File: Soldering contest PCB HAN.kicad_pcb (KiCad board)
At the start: 2 copper layers, 99.1 x 98.6 mm, 18 parts, among them J1 Screw_Terminal_01x02, Q1 2N3904, Q2 2N3904

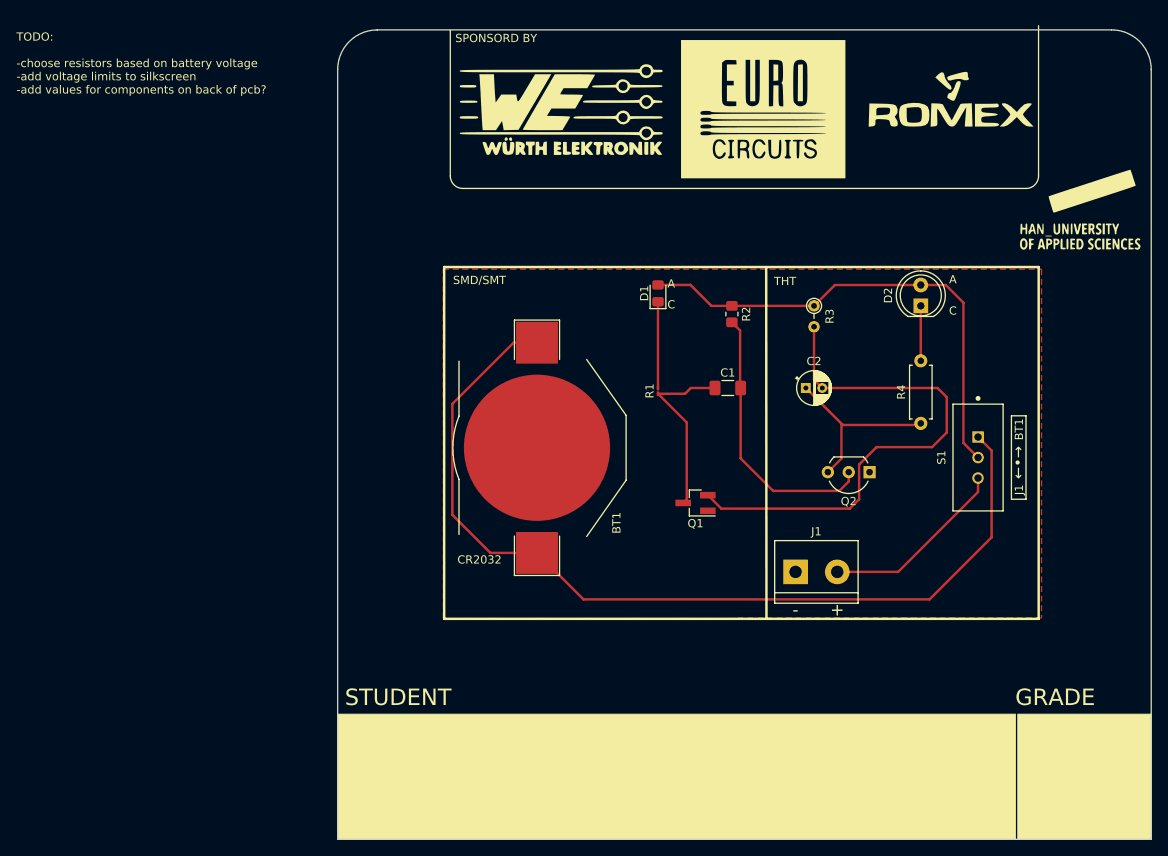
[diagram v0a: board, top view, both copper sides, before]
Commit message: added component values to silkscreen
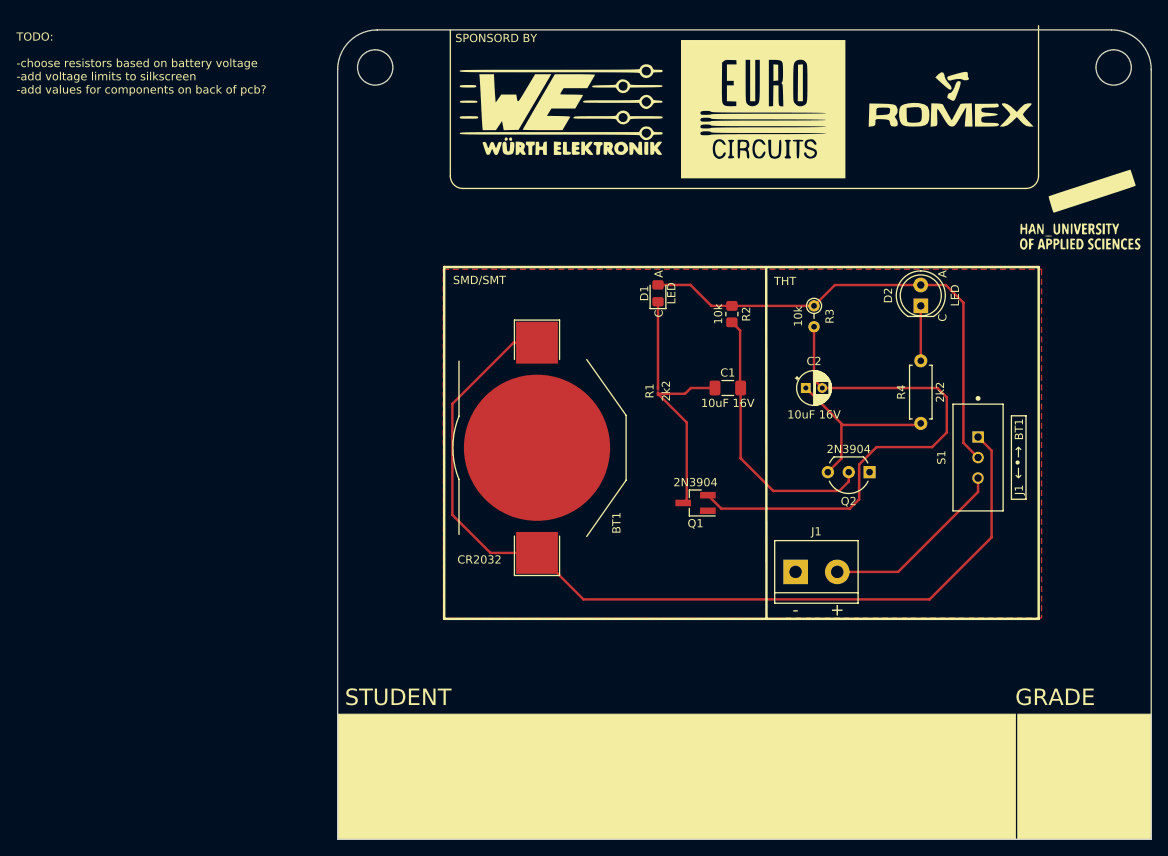
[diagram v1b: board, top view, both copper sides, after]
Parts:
- added REF**: KiCad-Logo2_12mm_SilkScreen, Symbol:KiCad-Logo2_12mm_SilkScreen, B.Cu at (138.2, 109.5)
- added hole1: MountingHole_4.3mm_M4, MountingHole:MountingHole_4.3mm_M4, F.Cu at (115.8, 55.9)
- added hole2: MountingHole_4.3mm_M4, MountingHole:MountingHole_4.3mm_M4, F.Cu at (205.7, 55.9)
- moved G*** 11.2 mm to (137.2, 83.3)
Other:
- board text added: "Project: Astable multivibrator Version: 0.1 Date: 18-11-2022 Documentation: https://gitlab.com/wlgrw/2023-ese-day-soldering-contest.git Designed for: ESE-day 27 January 2023 soldering contest Designed by: Casper R. Tak"
- board text removed: "Project: Astable multivibrator Version: 0.1 Date: 18-11-2022 Designed for: ESE-day 27 January 2023 soldering contest Designed by: Casper R. Tak"

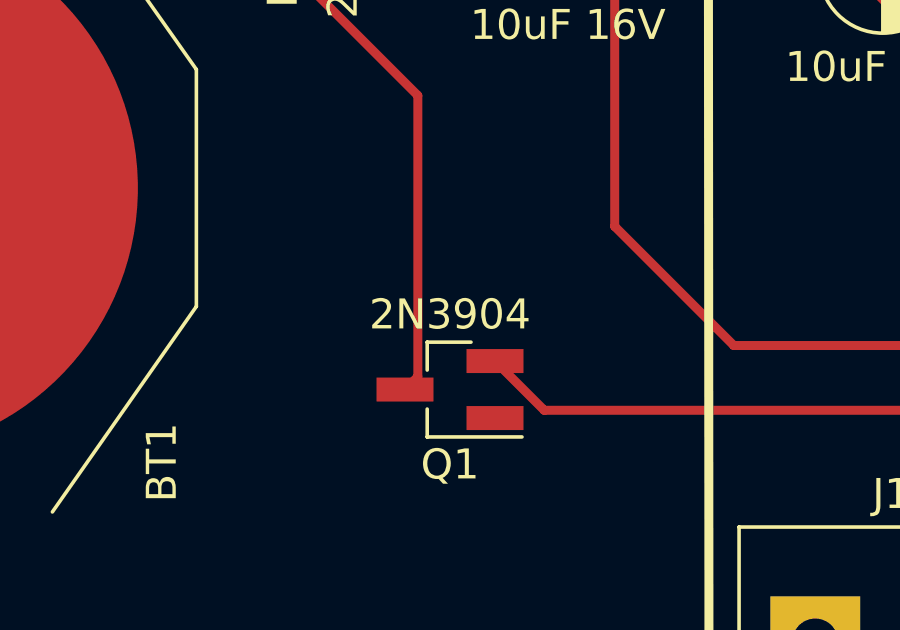
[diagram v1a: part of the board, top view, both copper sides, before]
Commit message: Finished V0.2
-added Remko's feedback
-changed a few component names to their smd parts
-added gitlab repo link to pcb (not yet uploaded to gitlab)
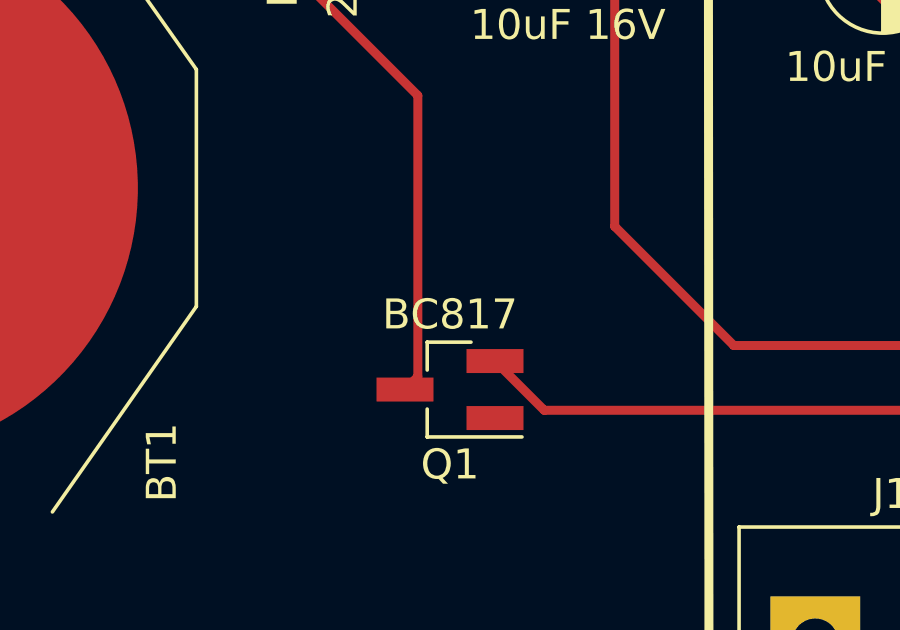
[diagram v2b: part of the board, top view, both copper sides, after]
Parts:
- Q1: value 2N3904 -> BC817
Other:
- board text added: "Project: Astable multivibrator Version: 0.2 Date: 18-11-2022 Documentation: https://gitlab.com/wlgrw/2023-ese-day-soldering-contest.git Designed for: ESE-day 27 January 2023 soldering contest Designed by: Casper R. Tak"
- board text removed: "Project: Astable multivibrator Version: 0.1 Date: 18-11-2022 Documentation: https://gitlab.com/wlgrw/2023-ese-day-soldering-contest.git Designed for: ESE-day 27 January 2023 soldering contest Designed by: Casper R. Tak"
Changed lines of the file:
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@@
       (effects (font (size 1.000685 1.000685) (thickness 0.15)))
     )
-    (fp_text value "SWITCH-SPDT-PTH-11.6X4.0MM-KIT" (at 1.12136 4.170085 90) (layer "F.Fab")
+    (fp_text value "SWITCH-SPDT-PTH-11.6X4.0MM-KIT" (at 0 -7.366 90) (layer "F.Fab")
       (effects (font (size 1.00122 1.00122) (thickness 0.15)))
     )
@@
       (effects (font (size 1 1) (thickness 0.15)))
     )
-    (fp_text value "Screw_Terminal_01x02" (at 2.54 5.08) (layer "F.Fab")
+    (fp_text value "Screw_Terminal_01x02" (at 5.207 -6.559) (layer "F.Fab")
       (effects (font (size 1 1) (thickness 0.15)))
     )
@@
       (effects (font (size 1 1) (thickness 0.15)))
     )
-    (fp_text value "2N3904" (at 0 2.5) (layer "F.SilkS")
+    (fp_text value "BC817" (at 0 2.5) (layer "F.SilkS")
       (effects (font (size 1 1) (thickness 0.15)))
     )
@@
     (effects (font (size 3.5 3.5) (thickness 0.5)) (justify left mirror))
   )
-  (gr_text "Project: Astable multivibrator\nVersion: 0.1\nDate: 18-11-2022\nDocumentation: https://gitlab.com/wlgrw/2023-ese-day-soldering-contest.git\n\nDesigned for: ESE-day 27 January 2023 soldering contest\nDesigned by: Casper R. Tak" (at 208.28 140.208) (layer "B.SilkS")
+  (gr_text "Project: Astable multivibrator\nVersion: 0.2\nDate: 18-11-2022\nDocumentation: https://gitlab.com/wlgrw/2023-ese-day-soldering-contest.git\n\nDesigned for: ESE-day 27 January 2023 soldering contest\nDesigned by: Casper R. Tak" (at 208.28 140.208) (layer "B.SilkS")
     (effects (font (size 1.5 1.5) (thickness 0.2)) (justify left mirror))
   )

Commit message: improved values
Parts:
- removed REF**: KiCad-Logo2_12mm_SilkScreen, Symbol:KiCad-Logo2_12mm_SilkScreen
- removed hole1, hole2: MountingHole_4.3mm_M4, MountingHole:MountingHole_4.3mm_M4
- R1, R4: value 2k2 -> 400
- R2, R3: value 10k -> 200k
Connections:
- D1 pad 1: Net-(D1-Pad1) -> Net-(C1-Pad1)
- D1 pad 2: Net-(D1-Pad2) -> Net-(R1-Pad1)
- D2 pad 1: Net-(D2-Pad1) -> Net-(C2-Pad1)
- D2 pad 2: Net-(D1-Pad2) -> Net-(R4-Pad1)
- R1 pad 1: Net-(C1-Pad1) -> Net-(R1-Pad1)
- R1 pad 2: Net-(D1-Pad1) -> Net-(R1-Pad2)
- R2 pad 1: Net-(D1-Pad2) -> Net-(R1-Pad2)
- R3 pad 1: Net-(D1-Pad2) -> Net-(R1-Pad2)
- R4 pad 1: Net-(C2-Pad1) -> Net-(R4-Pad1)
- R4 pad 2: Net-(D2-Pad1) -> Net-(R1-Pad2)
- S1 pad 2: Net-(D1-Pad2) -> Net-(R1-Pad2)
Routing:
- net Net-(R1-Pad2): track 0.00 -> 77.0 mm
- net Net-(D1-Pad2): track 59.8 -> 0.00 mm
- net Net-(D1-Pad1): track 10.5 -> 0.00 mm
- net Net-(D2-Pad1): track 6.69 -> 0.00 mm

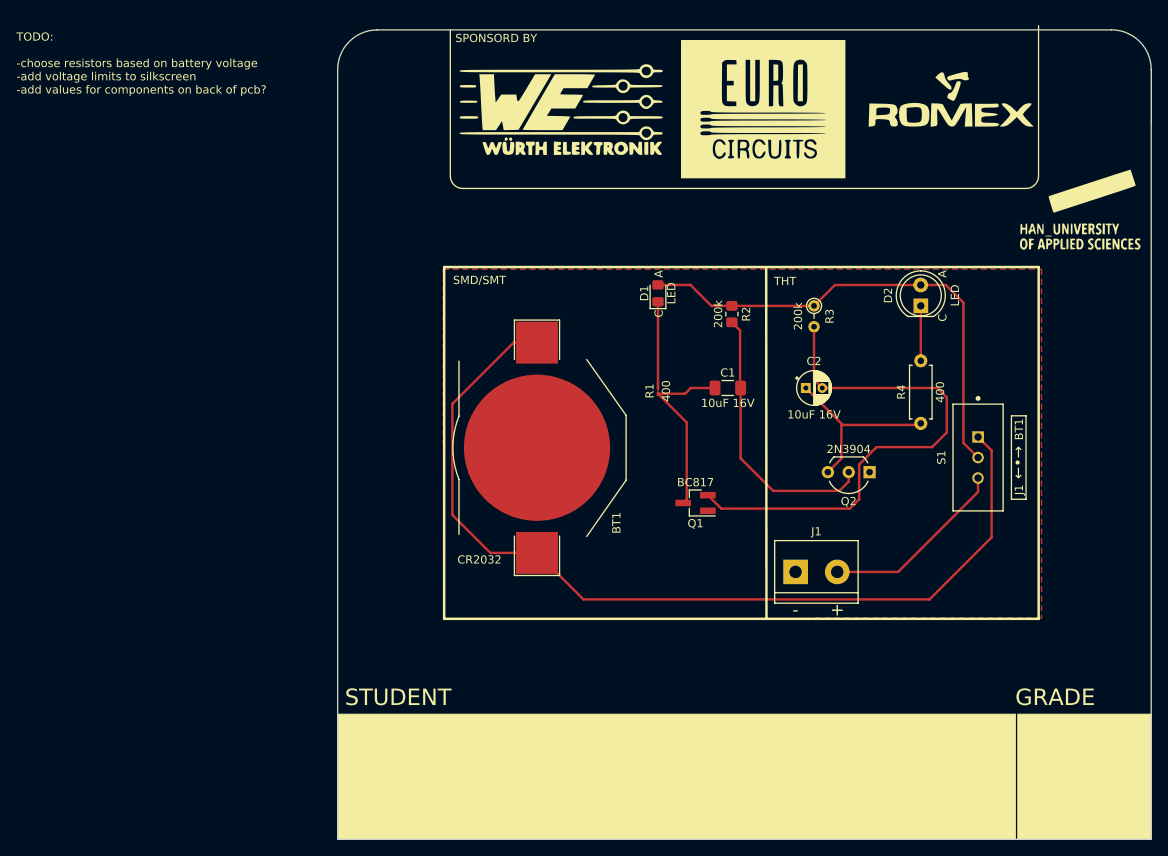
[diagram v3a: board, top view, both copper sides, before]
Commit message: Added the correct values to the components
-R val
-C val
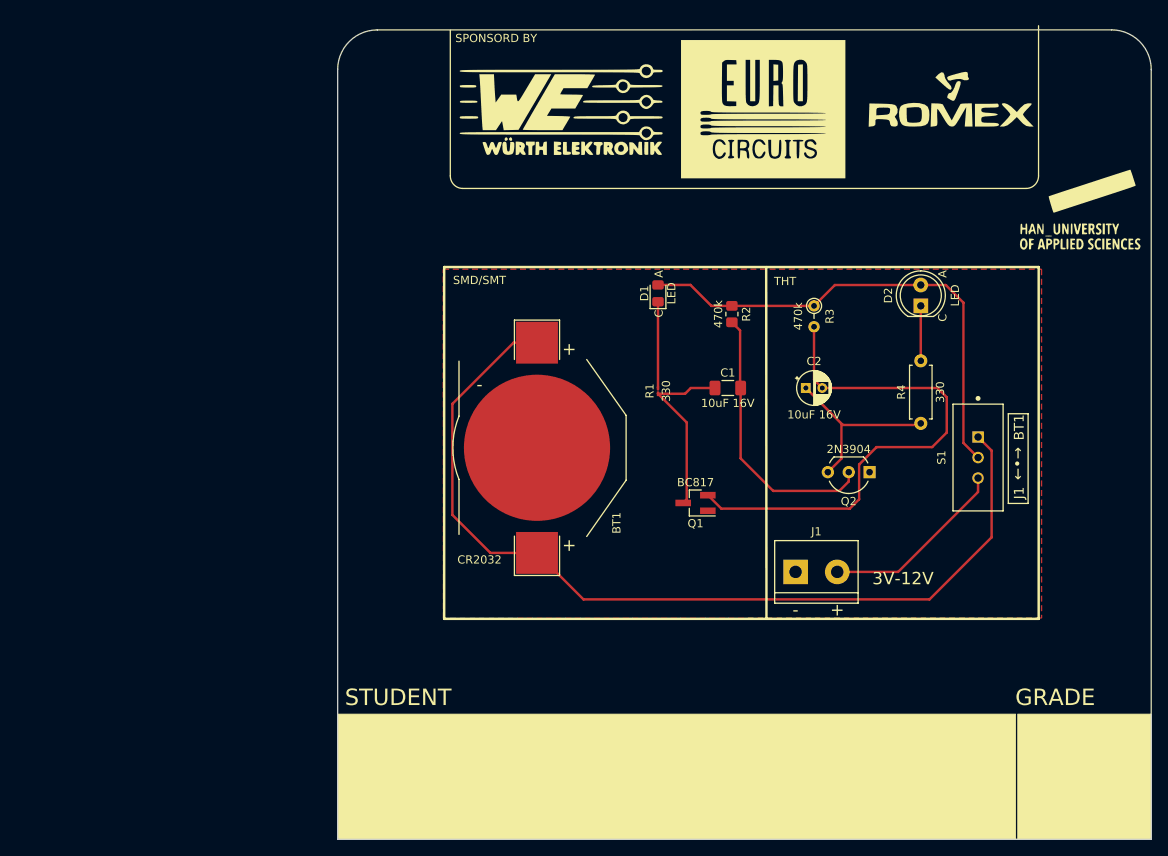
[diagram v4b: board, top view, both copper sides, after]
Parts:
- R1, R4: value 400 -> 330
- R2, R3: value 200k -> 470k
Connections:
- D1 pad 1: Net-(C1-Pad1) -> Net-(D1-Pad1)
- D1 pad 2: Net-(R1-Pad1) -> Net-(D1-Pad2)
- D2 pad 1: Net-(C2-Pad1) -> Net-(D2-Pad1)
- D2 pad 2: Net-(R4-Pad1) -> Net-(D1-Pad2)
- R1 pad 1: Net-(R1-Pad1) -> Net-(C1-Pad1)
- R1 pad 2: Net-(R1-Pad2) -> Net-(D1-Pad1)
- R2 pad 1: Net-(R1-Pad2) -> Net-(D1-Pad2)
- R3 pad 1: Net-(R1-Pad2) -> Net-(D1-Pad2)
- R4 pad 1: Net-(R4-Pad1) -> Net-(C2-Pad1)
- R4 pad 2: Net-(R1-Pad2) -> Net-(D2-Pad1)
- S1 pad 2: Net-(R1-Pad2) -> Net-(D1-Pad2)
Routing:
- net Net-(R1-Pad2): track 77.0 -> 0.00 mm
- net Net-(D1-Pad2): track 0.00 -> 59.8 mm
- net Net-(D1-Pad1): track 0.00 -> 10.5 mm
- net Net-(D2-Pad1): track 0.00 -> 6.69 mm
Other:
- board text added: "3V-12V"
- board text removed: "TODO: -choose resistors based on battery voltage -add voltage limits to silkscreen -add values for components on back of pcb?"

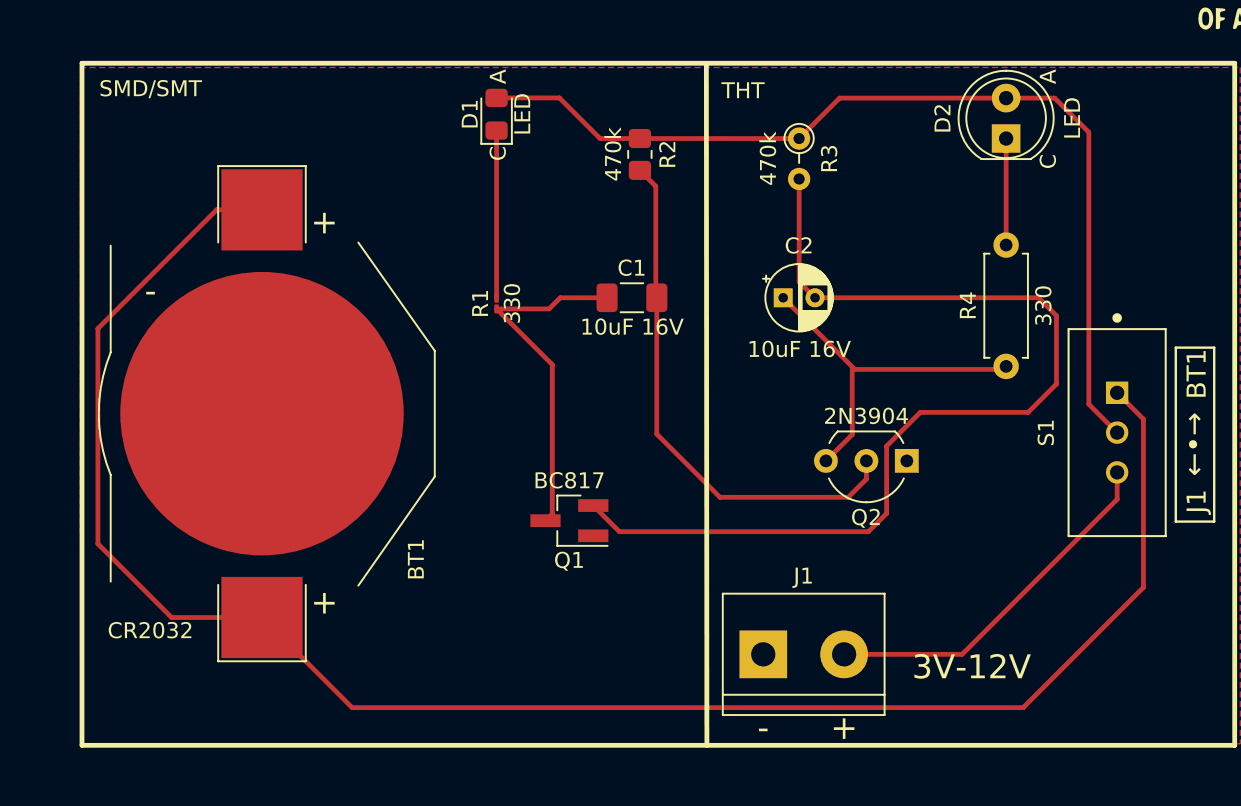
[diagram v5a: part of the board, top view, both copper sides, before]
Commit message: added rounded tracks version of V0.2
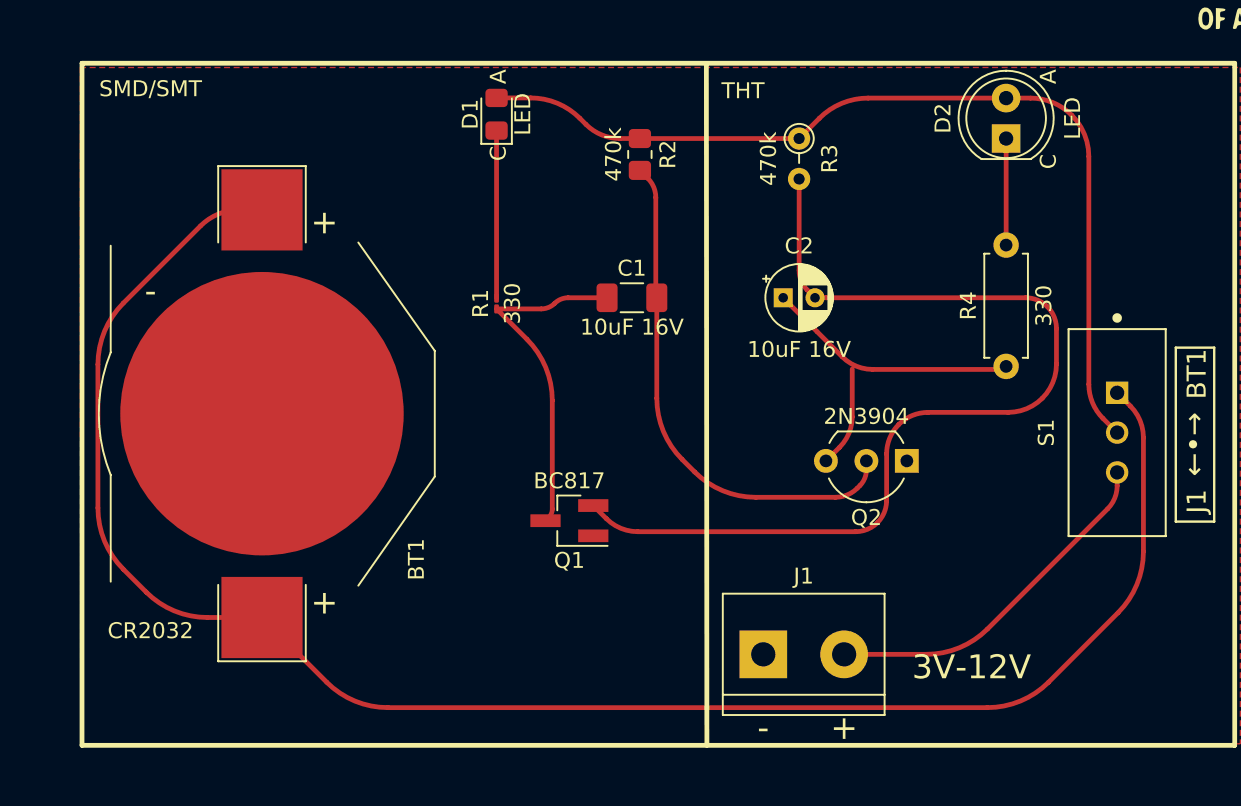
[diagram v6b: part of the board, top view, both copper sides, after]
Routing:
- net Net-(BT1-Pad1): track 112.9 -> 111.0 mm
- net Net-(D1-Pad2): track 59.8 -> 58.7 mm
- net Net-(C2-Pad2): track 63.9 -> 63.0 mm
- net Net-(C1-Pad2): track 33.4 -> 32.6 mm

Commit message: small improvements on silkscreen
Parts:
- added REF**: KiCad-Logo2_12mm_SilkScreen, Symbol:KiCad-Logo2_12mm_SilkScreen, B.Cu at (138.4, 110.8)
